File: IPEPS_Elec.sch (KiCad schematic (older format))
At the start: 25 parts

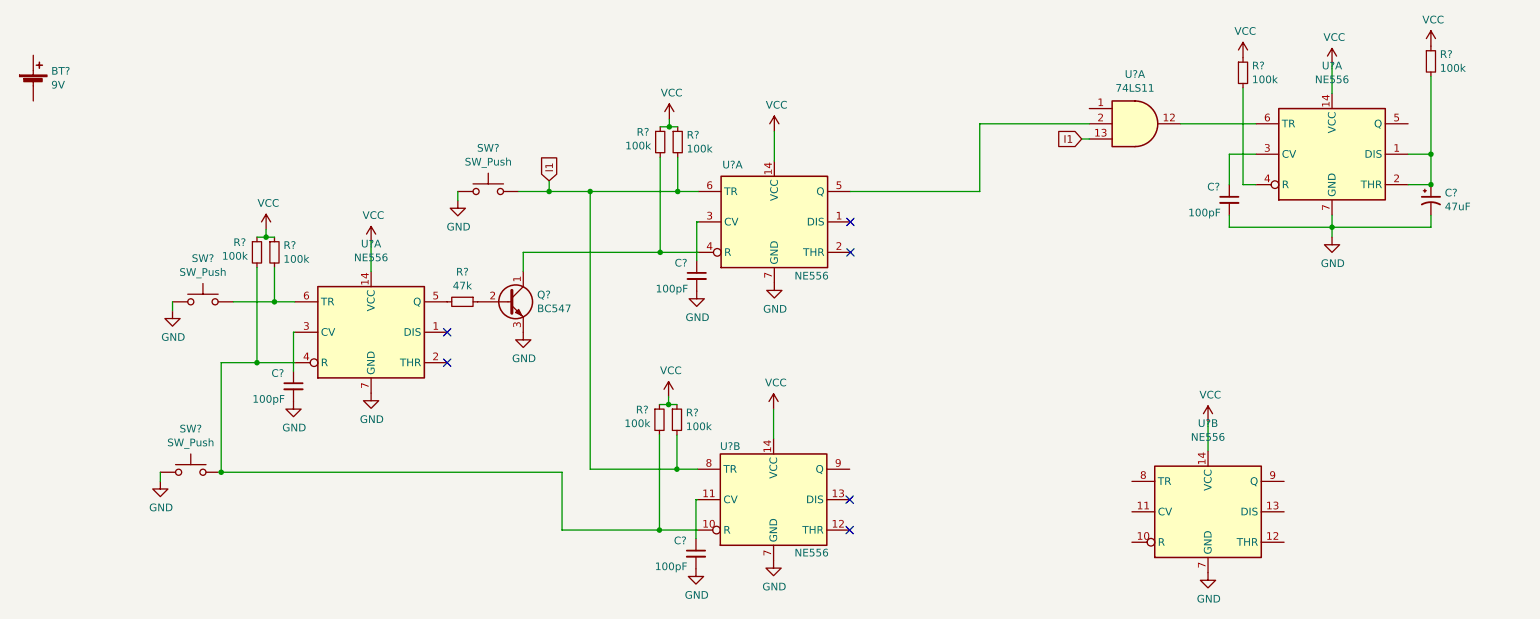
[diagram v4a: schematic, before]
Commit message: add output LEDs
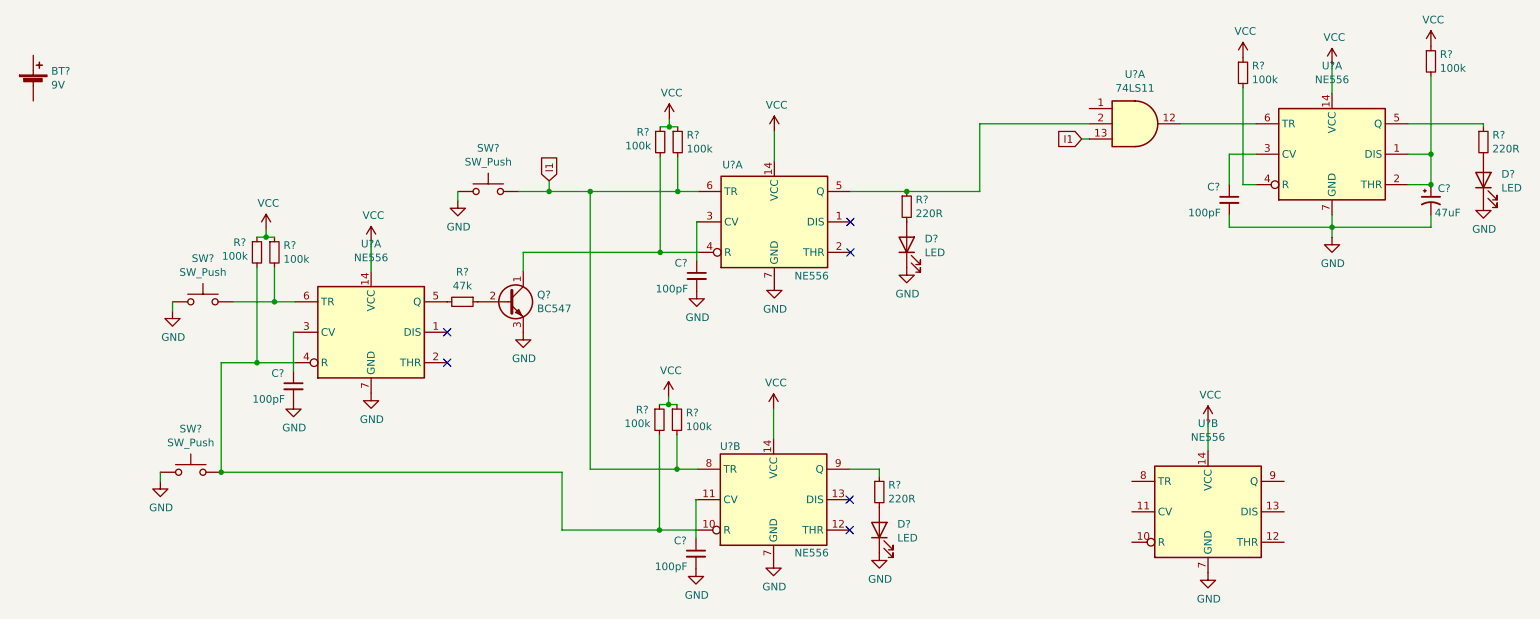
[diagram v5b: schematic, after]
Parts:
- added D? (x3): LED, symbol Device:LED
- added R? (x3): 220R, symbol Device:R_Small
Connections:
- net GND: now also D?.1 (K), D?.1 (K), D?.1 (K)
- net at U?.2, U?.5 (Q): now also R?.1
- net at U?.9 (Q): now also R?.1
- net at U?.5 (Q): now also R?.1
- new net: D?.2 (A), R?.2 (x3)
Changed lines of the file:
@@
 U 1 1 619F6519
 P 10275 1915
-F 0 "C?" H 10366 1961 50  0000 L CNN
-F 1 "47uF" H 10366 1870 50  0000 L CNN
+F 0 "C?" H 10320 1990 50  0000 L CNN
+F 1 "47uF" H 10300 1830 50  0000 L CNN
 F 2 "" H 10275 1915 50  0001 C CNN
 F 3 "~" H 10275 1915 50  0001 C CNN
@@
 	8030 1515 7980 1515
 Wire Wire Line
-	6460 1860 7310 1860
+	6460 1860 6830 1860
 Wire Wire Line
 	7310 1860 7310 1415
@@
 	1    0    0    -1
 $EndComp
+$Comp
+L Device:R_Small R?
+U 1 1 61A2FF9C
+P 6650 3835
+F 0 "R?" H 6709 3881 50  0000 L CNN
+F 1 "220R" H 6709 3790 50  0000 L CNN
+F 2 "" H 6650 3835 50  0001 C CNN
+F 3 "~" H 6650 3835 50  0001 C CNN
+	1    6650 3835
+	1    0    0    -1
+$EndComp
+$Comp
+L Device:R_Small R?
+U 1 1 61A30870
+P 6830 1960
+F 0 "R?" H 6889 2006 50  0000 L CNN
+F 1 "220R" H 6889 1915 50  0000 L CNN
+F 2 "" H 6830 1960 50  0001 C CNN
+F 3 "~" H 6830 1960 50  0001 C CNN
+	1    6830 1960
+	1    0    0    -1
+$EndComp
+Connection ~ 6830 1860
+Wire Wire Line
+	6830 1860 7310 1860
+Wire Wire Line
+	6650 3735 6650 3685
+Wire Wire Line
+	6650 3685 6455 3685
+$Comp
+L Device:R_Small R?
+U 1 1 61A351A1
+P 10620 1535
+F 0 "R?" H 10679 1581 50  0000 L CNN
+F 1 "220R" H 10679 1490 50  0000 L CNN
+F 2 "" H 10620 1535 50  0001 C CNN
+F 3 "~" H 10620 1535 50  0001 C CNN
+	1    10620 1535
+	1    0    0    -1
+$EndComp
+Wire Wire Line
+	10620 1435 10620 1415
+Wire Wire Line
+	10620 1415 10125 1415
+$Comp
+L Device:LED D?
+U 1 1 61A38DFF
+P 6830 2210
+F 0 "D?" V 6869 2092 50  0000 R CNN
+F 1 "LED" V 6778 2092 50  0000 R CNN
+F 2 "" H 6830 2210 50  0001 C CNN
+F 3 "~" H 6830 2210 50  0001 C CNN
+	1    6830 2210
+	0    -1   -1   0
+$EndComp
+$Comp
+L Device:LED D?
+U 1 1 61A3B736
+P 6650 4085
+F 0 "D?" V 6689 3967 50  0000 R CNN
+F 1 "LED" V 6598 3967 50  0000 R CNN
+F 2 "" H 6650 4085 50  0001 C CNN
+F 3 "~" H 6650 4085 50  0001 C CNN
+	1    6650 4085
+	0    -1   -1   0
+$EndComp
+$Comp
+L Device:LED D?
+U 1 1 61A3E4F7
+P 10620 1785
+F 0 "D?" V 10659 1667 50  0000 R CNN
+F 1 "LED" V 10568 1667 50  0000 R CNN
+F 2 "" H 10620 1785 50  0001 C CNN
+F 3 "~" H 10620 1785 50  0001 C CNN
+	1    10620 1785
+	0    -1   -1   0
+$EndComp
+$Comp
+L power:GND #PWR?
+U 1 1 61A40E93
+P 10620 1935
+F 0 "#PWR?" H 10620 1685 50  0001 C CNN
+F 1 "GND" H 10625 1762 50  0000 C CNN
+F 2 "" H 10620 1935 50  0001 C CNN
+F 3 "" H 10620 1935 50  0001 C CNN
+	1    10620 1935
+	1    0    0    -1
+$EndComp
+$Comp
+L power:GND #PWR?
+U 1 1 61A41B46
+P 6830 2360
+F 0 "#PWR?" H 6830 2110 50  0001 C CNN
+F 1 "GND" H 6835 2187 50  0000 C CNN
+F 2 "" H 6830 2360 50  0001 C CNN
+F 3 "" H 6830 2360 50  0001 C CNN
+	1    6830 2360
+	1    0    0    -1
+$EndComp
+$Comp
+L power:GND #PWR?
+U 1 1 61A43982
+P 6650 4235
+F 0 "#PWR?" H 6650 3985 50  0001 C CNN
+F 1 "GND" H 6655 4062 50  0000 C CNN
+F 2 "" H 6650 4235 50  0001 C CNN
+F 3 "" H 6650 4235 50  0001 C CNN
+	1    6650 4235
+	1    0    0    -1
+$EndComp

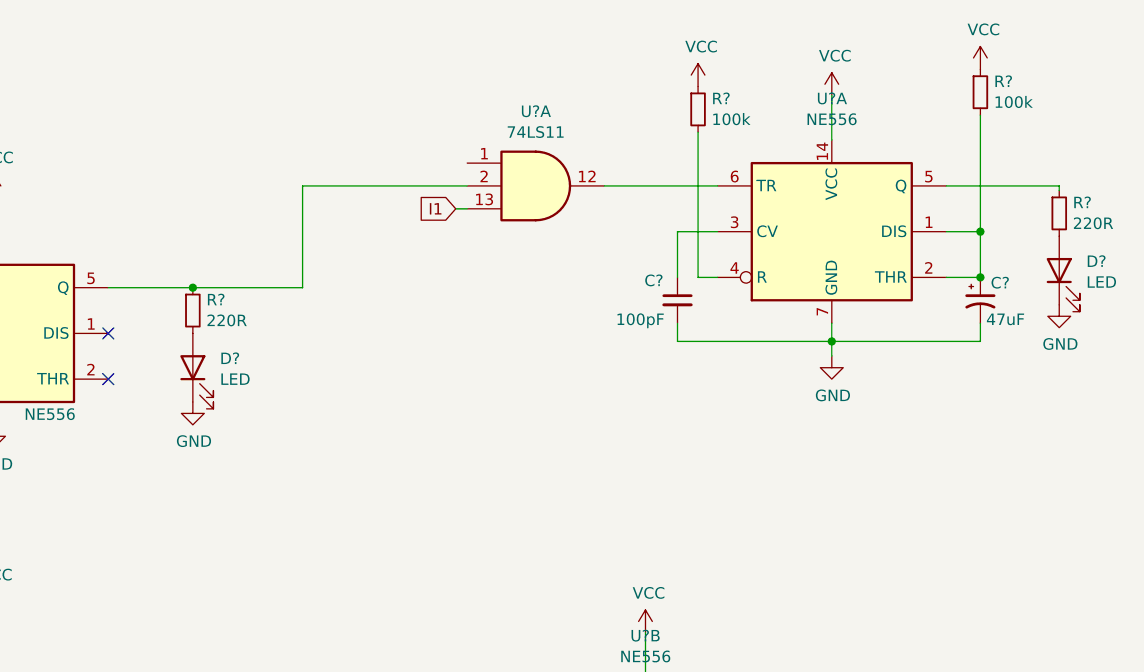
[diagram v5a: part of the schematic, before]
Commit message: add inverted O3 as AND input
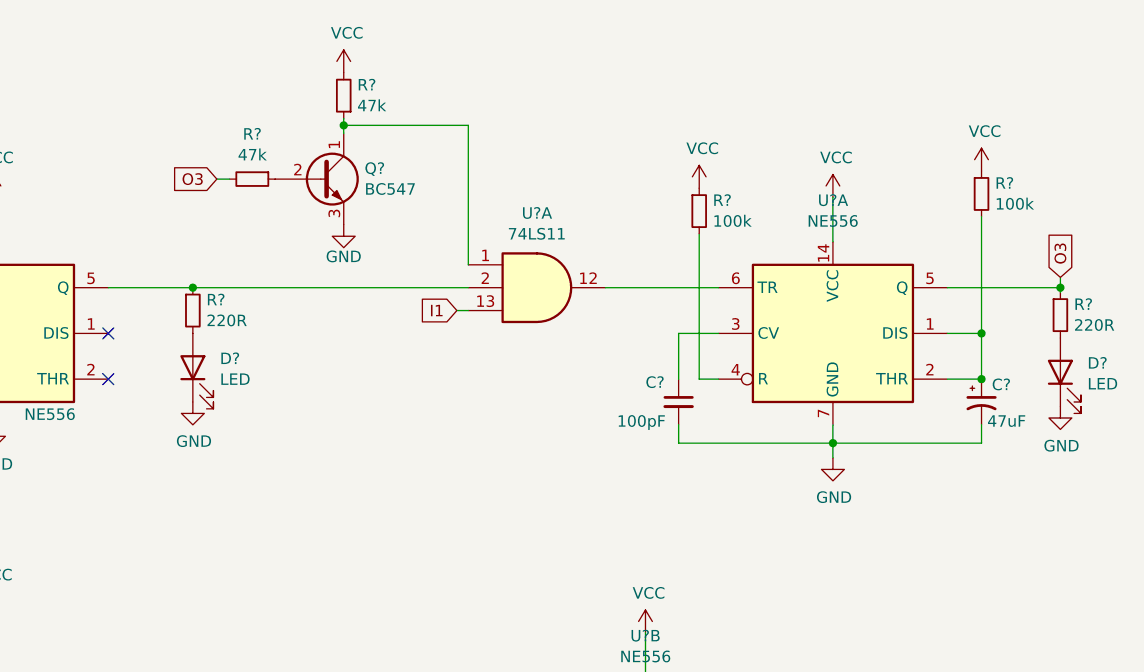
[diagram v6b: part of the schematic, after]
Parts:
- added Q?: BC547, Package_TO_SOT_THT:TO-92_Inline, symbol Transistor_BJT:BC547
- added R? (x2): 47k, symbol Device:R_Small
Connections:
- net GND: now also Q?.3 (E)
- net VCC: now also R?.2
- net O3: now reaches R?.1, U?.5 (Q)
- net O3: now also R?.2
- net at U?.1: now also Q?.1 (C), R?.1
- new net: Q?.2 (B), R?.1
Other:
- moved on the sheet: C?, D?, R?, U?A

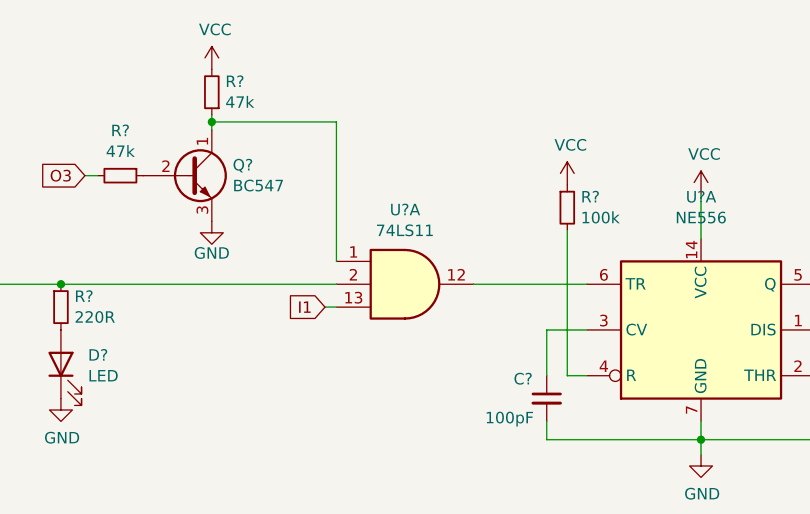
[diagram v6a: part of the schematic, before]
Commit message: change AND IC
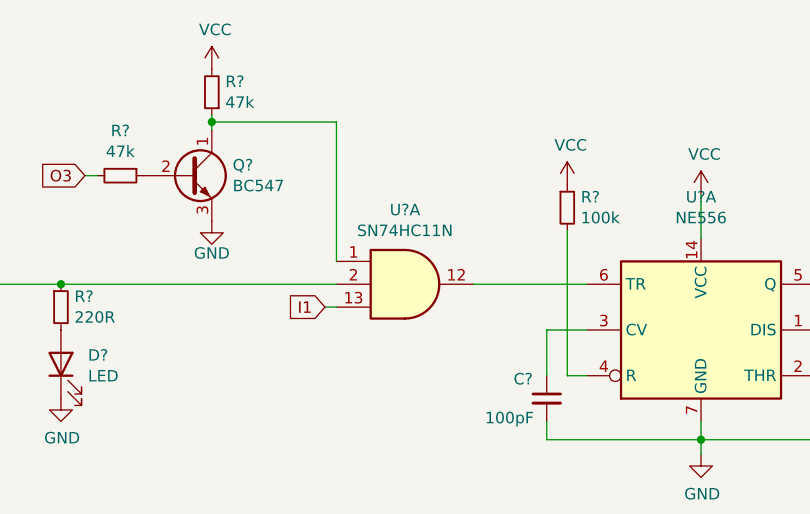
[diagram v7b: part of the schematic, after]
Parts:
- U?: value 74LS11 -> SN74HC11N
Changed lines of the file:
@@
 P 8335 1860
 F 0 "U?" H 8335 2185 50  0000 C CNN
-F 1 "74LS11" H 8335 2094 50  0000 C CNN
+F 1 "SN74HC11N" H 8335 2094 50  0000 C CNN
 F 2 "" H 8335 1860 50  0001 C CNN
-F 3 "http://www.ti.com/lit/gpn/sn74LS11" H 8335 1860 50  0001 C CNN
+F 3 "https://www.ti.com/lit/ds/scls084d/scls084d.pdf" H 8335 1860 50  0001 C CNN
 	1    8335 1860
 	1    0    0    -1

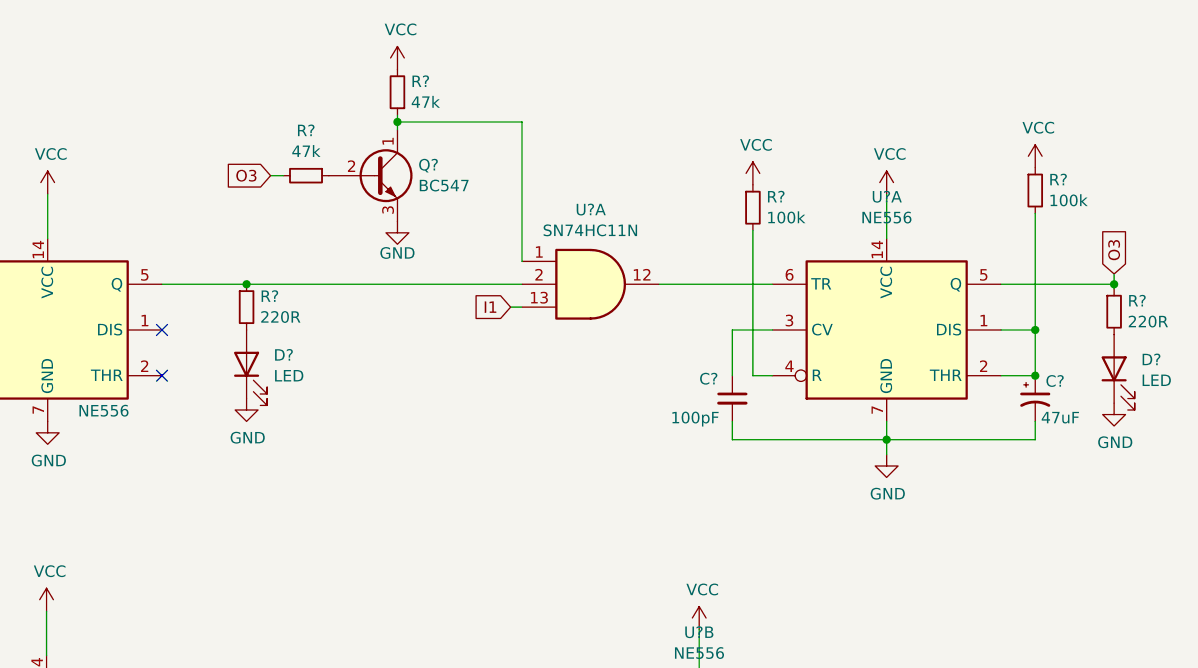
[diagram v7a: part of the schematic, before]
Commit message: fix the gate used for monostable timer input
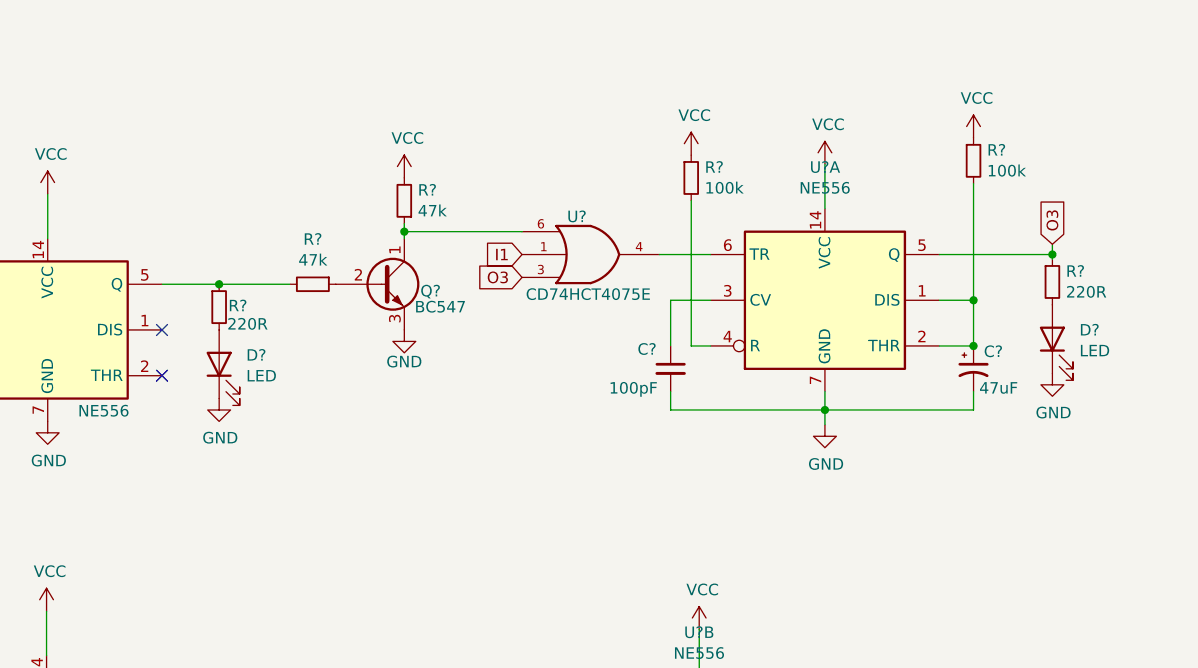
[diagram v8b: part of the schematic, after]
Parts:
- removed U?: SN74HC11N, symbol 74xx:74LS11
- added U?: CD74HCT4075E, symbol 74xGxx:74LVC1G332
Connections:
- net GND: now also U?.2 (GND)
- net I1: now also U?.1
- net O3: now also U?.3; no longer R?.2
- net VCC: now also U?.5 (VCC)
- net at R?.1, U?.5 (Q): now also R?.2
- net at U?.6 (TR): now also U?.4
- net at Q?.1 (C), R?.1: now also U?.6
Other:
- moved on the sheet: C?, D?, Q?, R?, U?A
